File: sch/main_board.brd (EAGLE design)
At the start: 160 x 100 mm, 0 parts

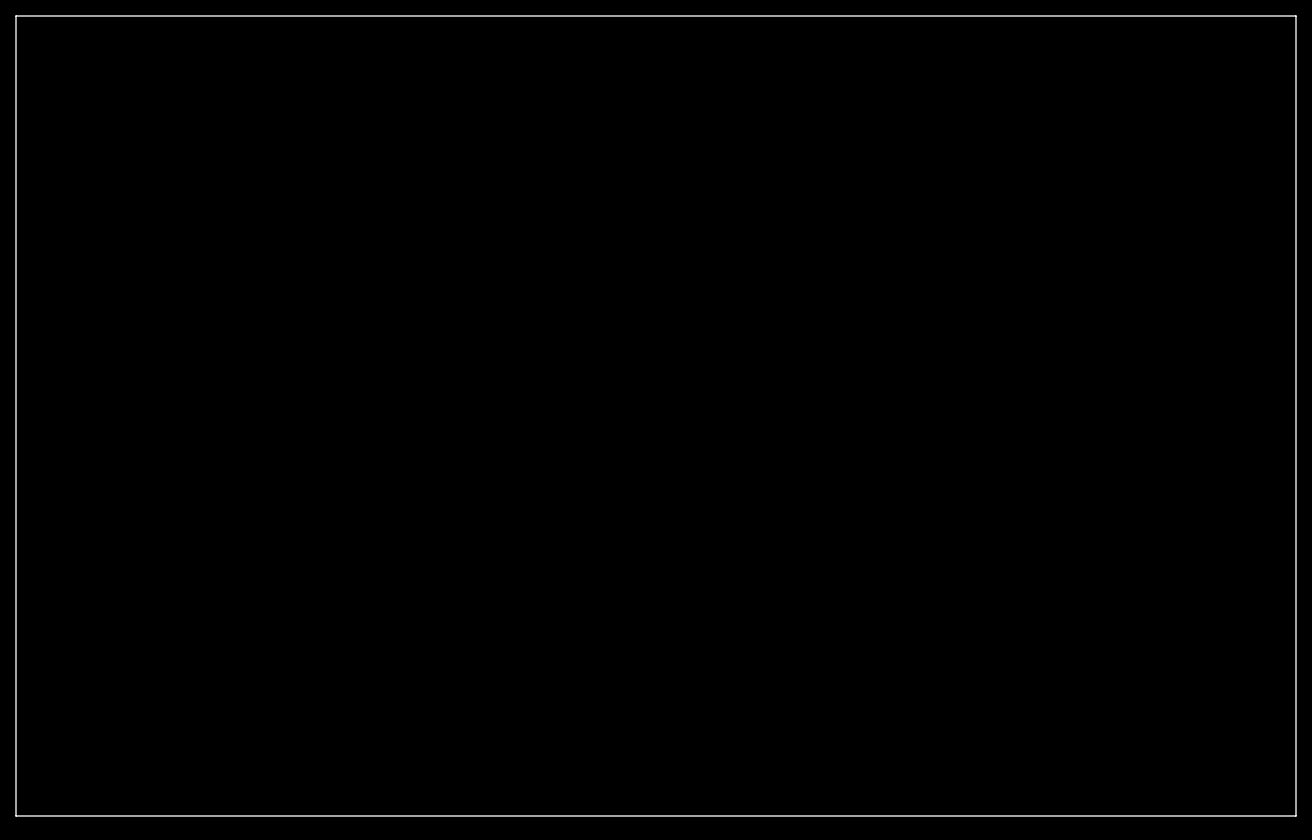
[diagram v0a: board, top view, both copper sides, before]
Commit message: - Add power supply for main board,
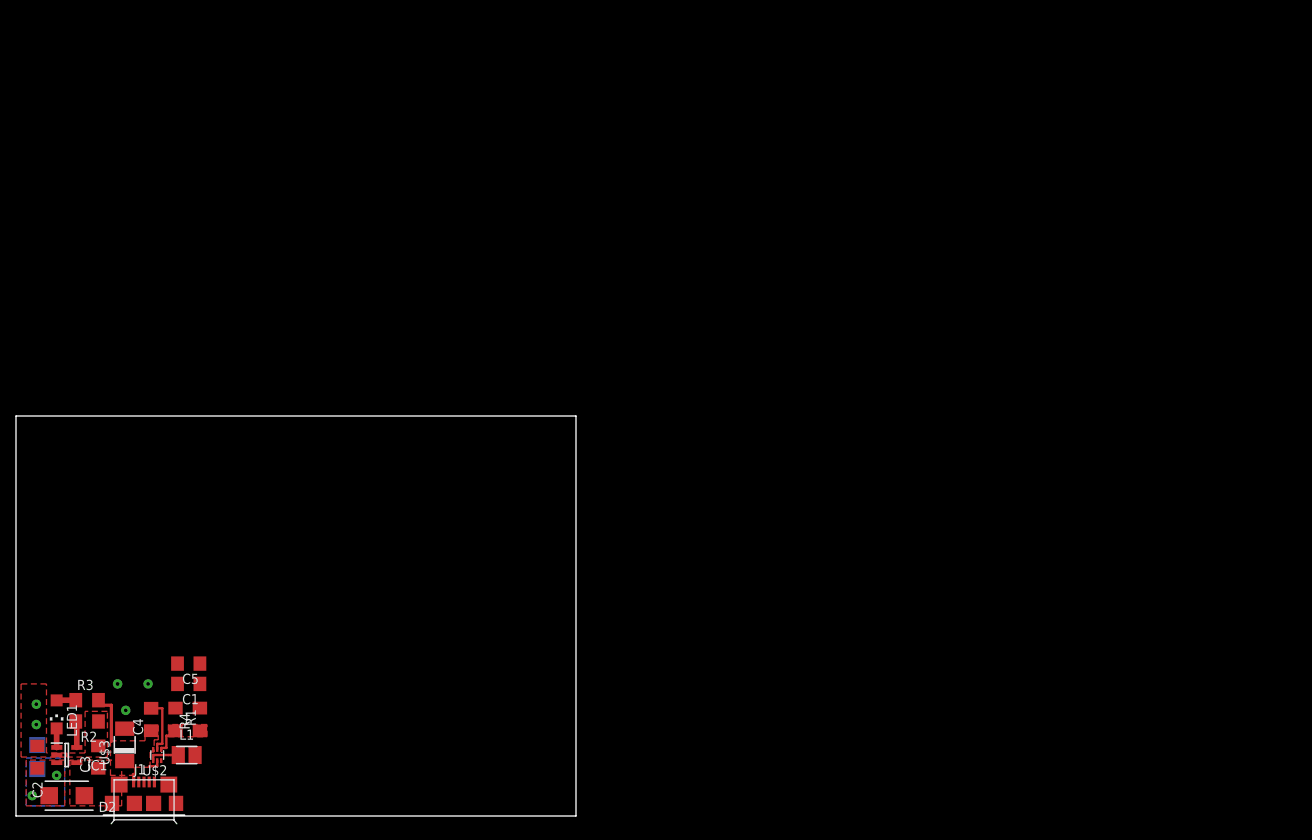
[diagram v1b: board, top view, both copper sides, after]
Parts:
- added C1, C2, C3, C4, C5: 4.7u, resistor:C1206
- added D2: VS-10BQ015-M3_5BT, SamacSys_Parts:DIOM5436X244N
- added IC1: MCP73831T-2ACI_OT, SamacSys_Parts:SOT95P270X145-5N
- added J1: MICRO_USB_B_HIROSE_ZX62-B-5PA(11), connector:USB_MICRO_B-HIROSE-ZX62-B-5PA(11)
- added L1: SRN2512-2R2M, SamacSys_Parts:INDPM2622X120N
- added LED1: GREEN, led:CHIPLED_1206
- added R1: 100k, resistor:R1206
- added R2: 10k, resistor:R1206
- added R3: 100, resistor:R1206
- added R4: 316k, resistor:R1206
- added U$1: BAT_FLAT_PAD, connector:BATTERY_FLAT_PAD
- added U$2: TLV62568DRLT, SamacSys_Parts:SOT563
- added U$3: SMAJ5.0A, SamacSys_Parts:DO-214AC
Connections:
- new net GND: C1.2, C2.2, C3.2, C4.2, C5.2, IC1.2, J1.5, R1.1, R2.1, U$1.M, U$2.2, U$3.A
- new net ID: J1.4
- new net N$1: LED1.A, R3.1
- new net N$2: IC1.1, LED1.C
- new net N$3: IC1.5, R2.2
- new net N$6: L1.1, U$2.4
- new net N$8: R1.2, R4.1, U$2.1
- new net USB_D+: J1.3
- new net USB_D-: J1.2
- new net VCC: C1.1, C5.1, L1.2, R4.2
- new net V_BATT: C2.1, D2.2, IC1.3, U$1.P
- new net V_USB: C3.1, C4.1, D2.1, IC1.4, J1.1, R3.2, U$2.3, U$2.5, U$3.C
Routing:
- net V_USB: track 0.00 -> 9.53 mm
- net GND: track 0.00 -> 7.18 mm, vias 0 -> 2
- net N$8: track 0.00 -> 3.87 mm
- net N$6: track 0.00 -> 3.83 mm
- net N$3: track 0.00 -> 3.30 mm
- net N$2: track 0.00 -> 2.40 mm
- net N$1: track 0.00 -> 2.40 mm
- added copper zone on layer 1, net GND
- added copper zone on layer 1, net N$8
- added copper zone on layer 1, net V_BATT
- added copper zone on layer 16, net V_BATT
- added copper zone on layer 1, net V_USB
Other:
- board size 160 x 100 mm -> 70 x 50 mm
